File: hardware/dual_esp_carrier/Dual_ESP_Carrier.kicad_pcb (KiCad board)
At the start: 2 copper layers, 100 x 100 mm, 39 parts, among them J1 ESP32_lafvin, J2 ESP32_B_LANDSCAPE, J3 SX1278_LORA_2x4, J6 GPS_LC29H_7PIN, SW1 subir ancora, SW2 MODE, SW3 largar ancora, SW4 BOOT

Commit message: feat: add Dual ESP32-C6 Over-The-Air (OTA) firmware update UI and bundling script
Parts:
- added J_EXP: EXPANSION, Connector_PinHeader_2.54mm:PinHeader_2x03_P2.54mm_Vertical, F.Cu at (64.0, 78.0)
- moved J3 8.46 mm to (86.0, 72.0)
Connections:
- J_DK_L pad 11: (no net) -> /EXP_IO11
- J_DK_L pad 8: (no net) -> /EXP_IO1
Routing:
- net /+3V3_C6: track 62.3 -> 82.2 mm
- net /EXP_IO1: track 0.00 -> 11.9 mm
- net /LORA_MISO: track 29.3 -> 38.2 mm
- net /LORA_NSS: track 22.2 -> 31.0 mm
- net /LORA_DIO0: track 24.1 -> 32.8 mm
- net /LORA_SCK: track 24.6 -> 33.1 mm
- net /LORA_MOSI: track 23.1 -> 31.5 mm
- net /EXP_IO11: track 0.00 -> 6.84 mm
- net /+5V: track 130.7 -> 137.5 mm
- net /LORA_RST: track 23.1 -> 29.7 mm
- net /WATER_SENS: track 62.6 -> 56.8 mm
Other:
- board text added: "3V3"
- board text added: "5V"
- board text added: "IO1"
- board text added: "IO11"

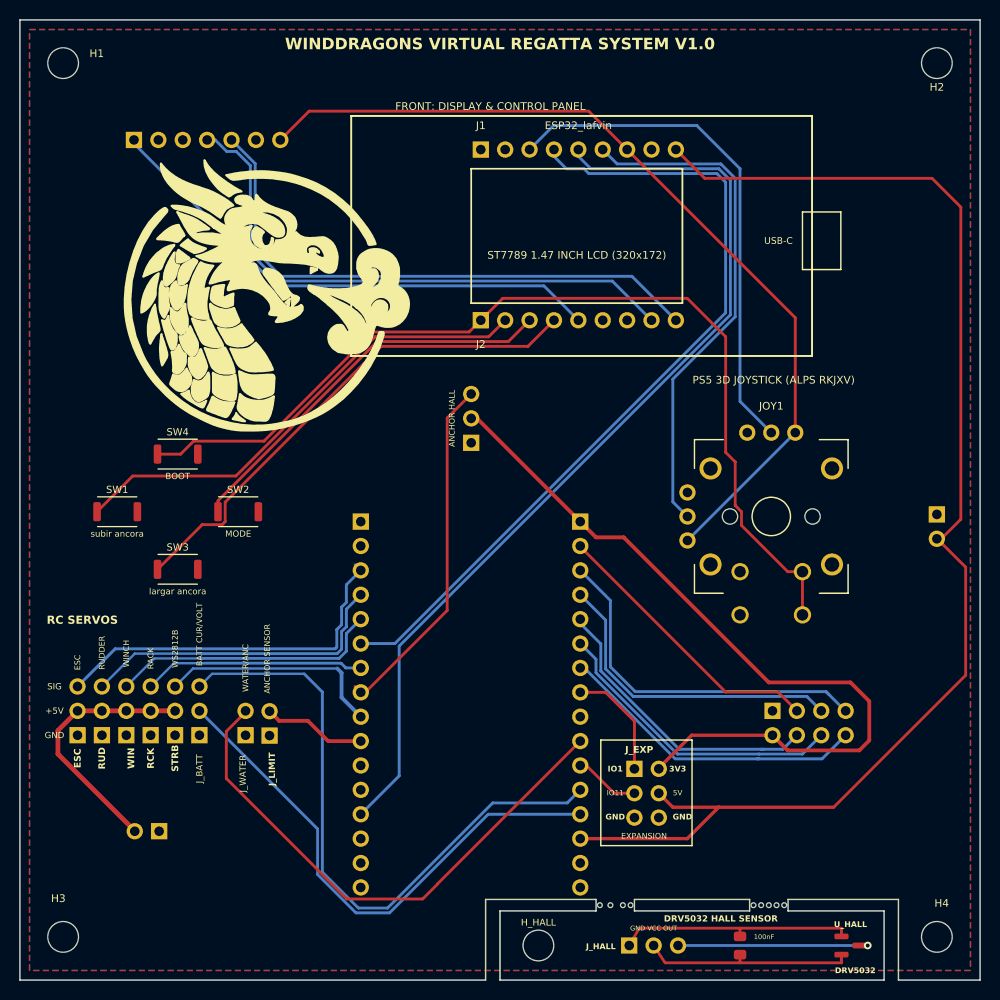
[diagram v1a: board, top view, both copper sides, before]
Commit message: update PCB layout and regenerate manufacturing gerbers and firmware archives
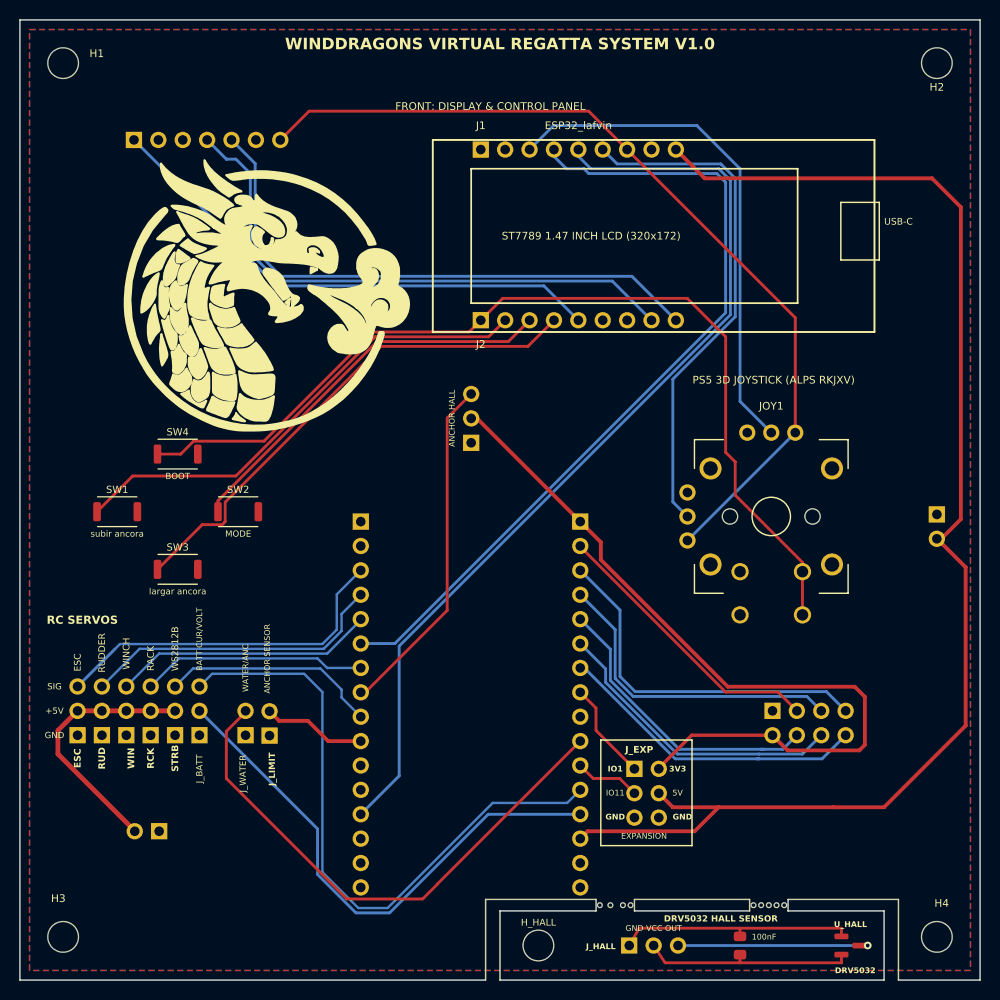
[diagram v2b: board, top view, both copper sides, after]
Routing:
- net /+5V: track 137.5 -> 140.6 mm
- net /SERVO_ESC: track 38.5 -> 36.7 mm
- net /EXP_IO1: track 11.9 -> 10.3 mm
- net /SERVO_RUDDER: track 33.1 -> 32.0 mm
- net /STROBE_DIN: track 23.7 -> 22.7 mm
- net /SERVO_WINCH: track 28.4 -> 27.4 mm
- net /IO9_BOOT: track 100.7 -> 99.8 mm
- net /ANCHOR_HALL: track 37.0 -> 36.1 mm
- net /+3V3_C6: track 82.2 -> 82.9 mm
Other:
- board text removed: "DIRECT LEDC PWM SERVOS"
